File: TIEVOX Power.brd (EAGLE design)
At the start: 62.5 x 54 mm, 15 parts, among them IC1 NE555P, T1 2N222A

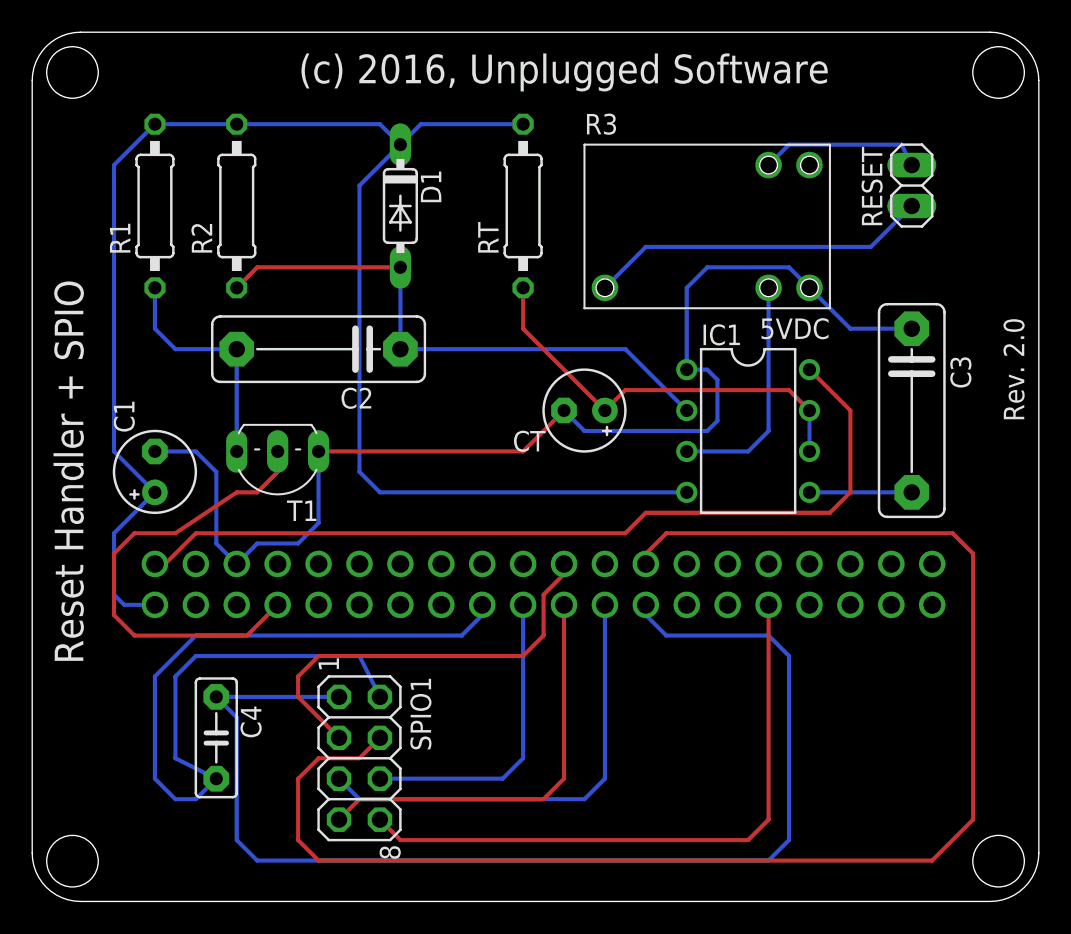
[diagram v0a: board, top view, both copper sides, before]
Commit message: Should have working versions of all required boards now.
Updated to No Commercial license.
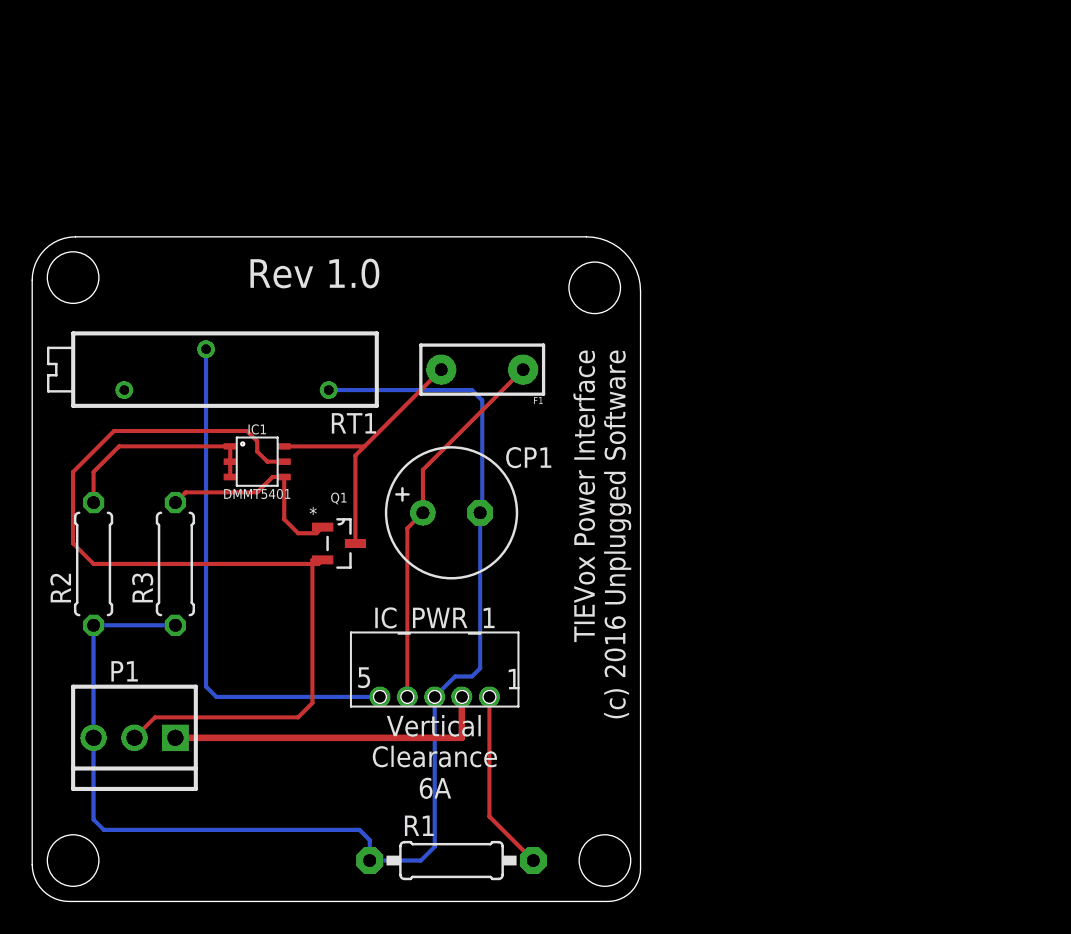
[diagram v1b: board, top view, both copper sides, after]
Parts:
- removed C1: 47uF, rcl:E2,5-5
- removed C2, C3: 0.01uF, capacitor-wima:C10B4
- removed C4: 0.1uf, capacitor-wima:C5B2.5
- removed CT: 10uF, rcl:E2,5-5
- removed D1: 1N4148, diode:DO35-7
- removed GPIO1: RPI_GPIO_MALE_OPEN, connectors:RPI_GPIO_FEMALE_TOP
- removed RESET: (no value), pinhead:1X02
- removed RT: 10K, resistor:0207/10
- removed SPIO1: 2.4GHz, pinhead:2X04
- removed T1: 2N222A, transistor-neu-to92:TO92-EBC
- added CP1: 1000uF, rcl:E3,5-8
- added F1: 06R155BPR, SparkFun-PowerIC:PTC
- added IC_PWR_1: 6A, packages:NE12S
- added P1: Power, connector:PINHEAD-LOCK-3
- added Q1: DMP2305U-7, Diodes_Inc_By_element14_Batch_1:SOT103P240X110-3N
- added RT1: 10K, resistor:RTRIM3006P
- IC1: value NE555P -> DMMT5401; device linear:DIL08 -> Diodes_Inc_By_element14_Batch_1:DMMT5401
- R1: value 10K -> 2.2K; device resistor:0207/10 -> adafruit:0207/10
- R2: value 10K -> 10K, 1%; device resistor:0207/10 -> adafruit:0207/7
- R3: value 5VDC -> 47K, 1%; device te-connectivity:OUAZ-SS1* -> adafruit:0207/7
- moved R1 44.6 mm to (26.0, 2.54), turned to 0 degrees
- moved R3 39.1 mm to (8.89, 21.0), turned to 90 degrees
- moved IC1 30.5 mm to (14.0, 27.3)
- moved R2 23.9 mm to (3.81, 21.0)
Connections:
- removed net +3.3VDC: C1.+, D1.C, GPIO1.1_3.3VDC, IC1.4, R1.2, R2.2, RT.2
- removed net 14_GND: GPIO1.14_GND
- removed net 20_GND: GPIO1.20_GND
- removed net 30_GND: GPIO1.30_GND
- removed net 34_GND: GPIO1.34_GND
- removed net 39_GND: GPIO1.39_GND
- removed net 4_5VDC: GPIO1.4_5VDC
- removed net 9_GND: GPIO1.9_GND
- removed net N$1: C2.2, R1.1, T1.C
- removed net N$10: C4.2, GPIO1.17_3.3VDC, SPIO1.2
- removed net N$11: GPIO1.26_SPI0_CE1, SPIO1.4
- removed net N$12: GPIO1.19_SPI0_MOSI, SPIO1.6
- removed net N$13: GPIO1.21_SPI0_MISO, SPIO1.7
- removed net N$14: GPIO1.23_SPI0_SCLK, SPIO1.5
- removed net N$15: GPIO1.31_GPIO6, SPIO1.8
- removed net N$2: C2.1, D1.A, IC1.2, R2.1
- removed net N$3: CT.+, IC1.6, IC1.7, RT.1
- removed net N$4: GPIO1.2_5VDC, IC1.8
- removed net N$5: C3.2, IC1.5
- removed net N$6: R3.VIN, RESET.1
- removed net N$7: R3.VOUT_NO, RESET.2
- removed net N$8: GPIO1.7_GPIO4, T1.B
- removed net N$9: C4.1, GPIO1.25_GND, SPIO1.1
- removed net RESET_OUT: IC1.3, R3.COIL1
- new net +5VDC: IC1.E2, P1.2, Q1.2
- new net GND_PC: CP1.-, IC_PWR_1.GND, P1.3, R1.1, R2.1, R3.1, RT1.1
- new net IN: F1.P$2, IC1.E1, Q1.3
- new net N$28: CP1.+, F1.P$1, IC_PWR_1.VOUT
- new net N$29: IC_PWR_1.ENABLE, R1.2
- new net N$32: IC1.B1, IC1.B2, IC1.C1, R2.2
- new net PWR12_TRIM: IC_PWR_1.TRIM, RT1.2
- net GND: now also IC1.C2, Q1.1, R3.2; no longer C1.-, C3.1, CT.-, GPIO1.6_GND, IC1.1, R3.COIL2, T1.E
- net N$16: now also IC_PWR_1.VIN, P1.1; no longer GPIO1.22_GPIO25, SPIO1.3
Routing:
- net +3.3VDC: track 101.3 -> 0.00 mm
- net N$11: track 91.9 -> 0.00 mm
- net GND_PC: track 0.00 -> 79.8 mm
- net N$9: track 74.4 -> 0.00 mm
- net GND: track 73.6 -> 12.9 mm
- net +5VDC: track 0.00 -> 57.4 mm
- net N$10: track 56.5 -> 0.00 mm
- net N$4: track 53.7 -> 0.00 mm
- net N$15: track 38.5 -> 0.00 mm
- net N$2: track 35.1 -> 0.00 mm
- net PWR12_TRIM: track 0.00 -> 32.0 mm
- net N$8: track 28.5 -> 0.00 mm
- net N$14: track 28.4 -> 0.00 mm
- net N$3: track 26.0 -> 0.00 mm
- net N$13: track 25.8 -> 0.00 mm
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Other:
- board size 62.5 x 54 mm -> 37.8 x 41.3 mm
- board text added: "Rev 1.0"
- board text added: "TIEVox Power Interface (c) 2016 Unplugged Software"
- board text removed: "(c) 2016, Unplugged Software"
- board text removed: "Reset Handler + SPIO"
- board text removed: "Rev. 2.0"
